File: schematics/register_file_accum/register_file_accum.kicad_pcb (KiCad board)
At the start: 2 copper layers, 100.1 x 91.1 mm, 31 parts, among them U1 74LS02, U2 74LS02, U3 74LS02, U4 74LS138, U5 74LS574, U6 74LS245, U7 74LS245, U8 74LS245

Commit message: silklayer check
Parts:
- moved kibuzzard-6911B41A 5.61 mm to (73.8, 78.8)

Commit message: power change
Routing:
- net GND: track 163.1 -> 190.3 mm
- net VCC: track 69.9 -> 94.1 mm, vias 1 -> 7

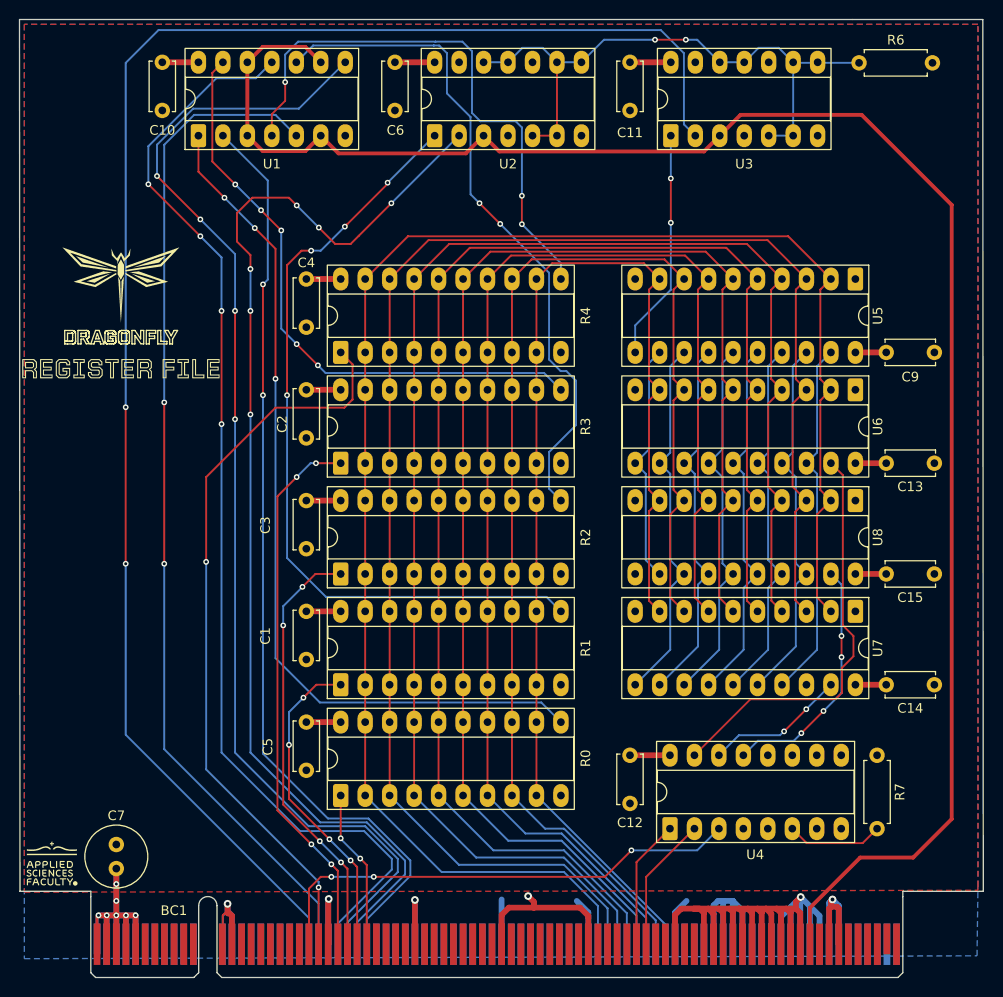
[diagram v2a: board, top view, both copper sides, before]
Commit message: fix: removed in control pins daisy chains
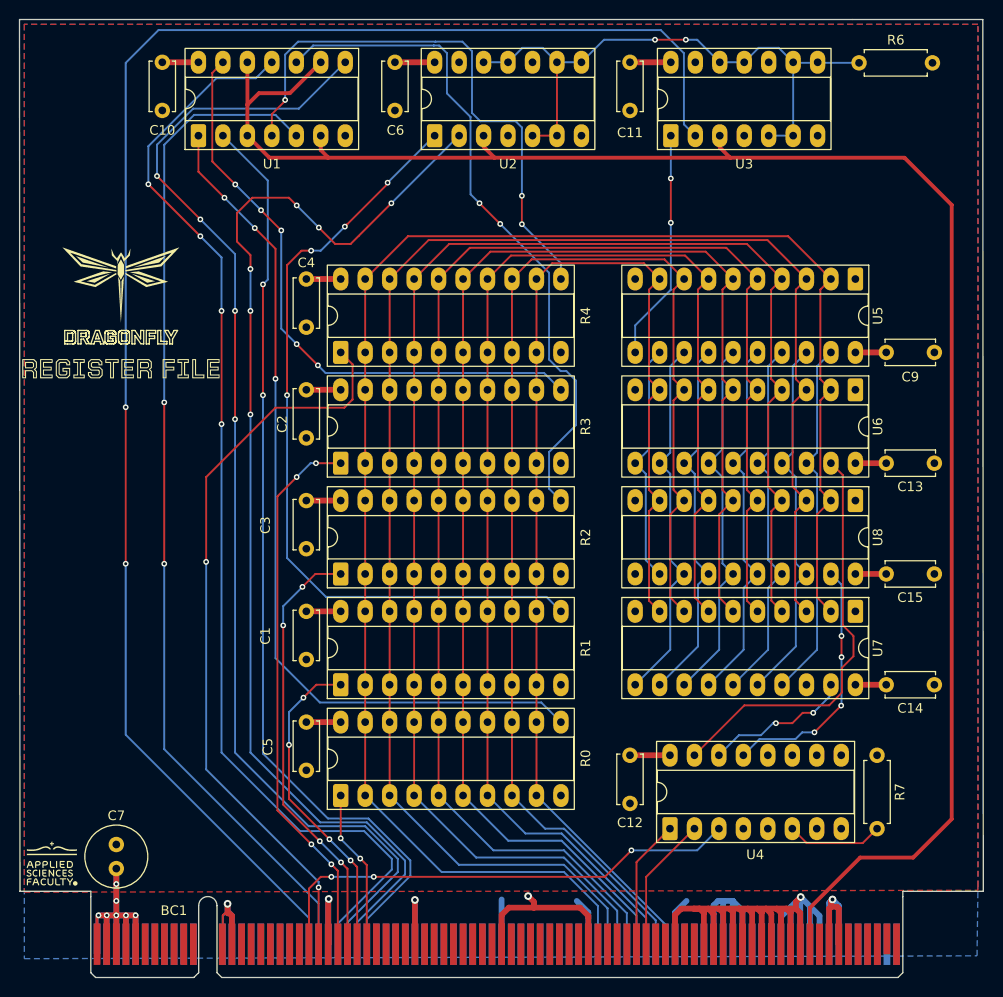
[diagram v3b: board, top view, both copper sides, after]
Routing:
- net /~{CLK}: track 184.7 -> 187.3 mm
- net /ACSHRIGHT: track 25.7 -> 26.4 mm
- net /ACSHLEFT: track 14.7 -> 15.3 mm

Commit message: fix(register_accum): fixed the data to y shape connection removed the vcc from the resistor
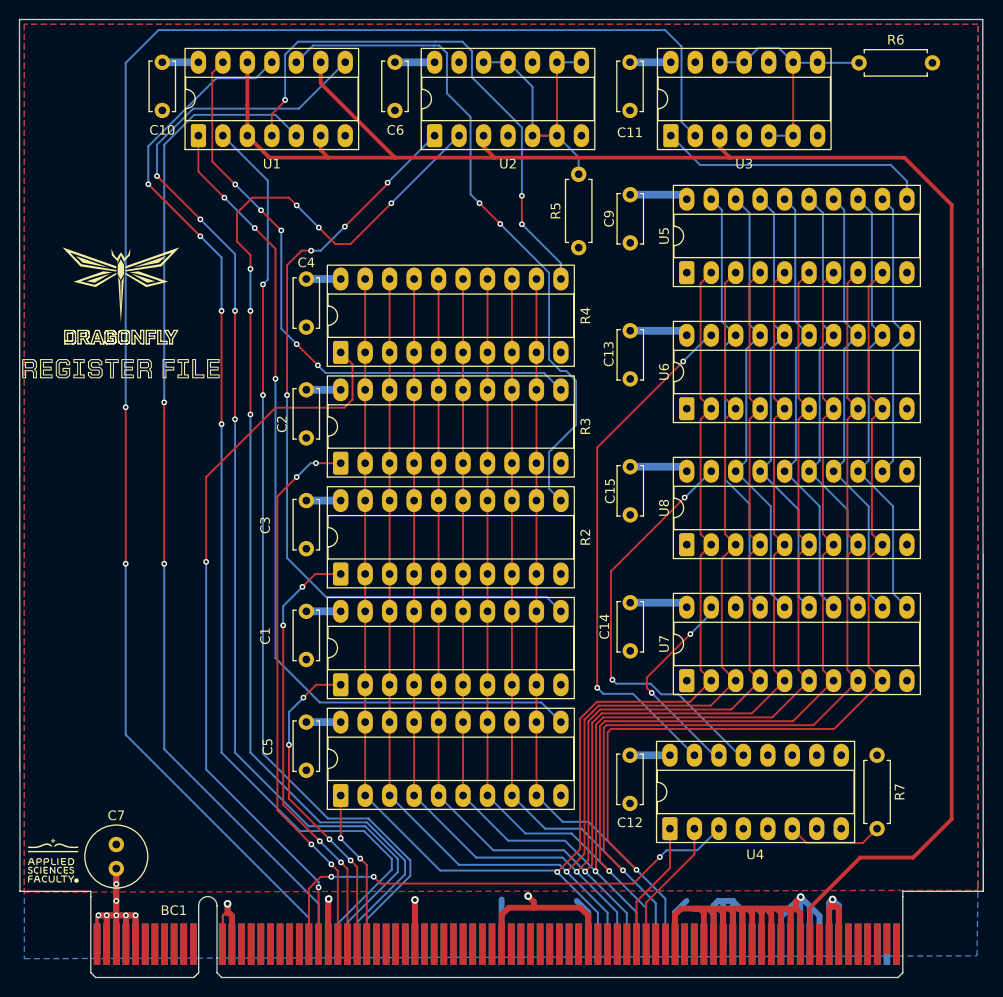
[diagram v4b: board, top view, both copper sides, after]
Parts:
- added R5: R, Resistor_THT:R_Axial_DIN0207_L6.3mm_D2.5mm_P7.62mm_Horizontal, F.Cu at (121.3, 66.2)
- moved C9 31.2 mm to (126.6, 60.7), turned to -90 degrees
- moved C13 29.9 mm to (126.6, 74.8), turned to -90 degrees
- moved C15 28.8 mm to (126.6, 88.9), turned to -90 degrees
- moved C14 27.9 mm to (126.6, 103.0), turned to -90 degrees
- moved U7 18.9 mm to (132.5, 111.1), turned to 90 degrees
- moved U8 18.1 mm to (132.5, 97.0), turned to 90 degrees
- moved U6 17.6 mm to (132.5, 82.9), turned to 90 degrees
- moved U5 17.5 mm to (132.5, 68.8), turned to 90 degrees
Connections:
- U2 pad 11: Net-(R6-Pad1) -> Net-(R5-Pad2)
- U2 pad 12: Net-(R6-Pad1) -> Net-(R5-Pad2)
- U2 pad 5: Net-(R6-Pad1) -> Net-(R5-Pad2)
- U2 pad 6: Net-(R6-Pad1) -> Net-(R5-Pad2)
- U2 pad 8: Net-(R6-Pad1) -> Net-(R5-Pad2)
- U2 pad 9: Net-(R6-Pad1) -> Net-(R5-Pad2)
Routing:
- net /DATA7: track 126.0 -> 168.1 mm, vias 0 -> 1
- net Net-(R6-Pad1): track 63.8 -> 25.9 mm, vias 2 -> 0
- net /DATA6: track 133.5 -> 166.6 mm, vias 0 -> 1
- net Net-(R5-Pad2): track 0.00 -> 31.0 mm
- net /DATA5: track 140.6 -> 165.4 mm, vias 0 -> 1
- net /ACSHRIGHT: track 26.4 -> 43.3 mm, vias 4 -> 2
- net /DATA4: track 147.7 -> 164.3 mm, vias 0 -> 1
- net /DATA0: track 176.1 -> 163.3 mm, vias 0 -> 1
- net /~{RAC}: track 43.3 -> 55.6 mm, vias 0 -> 2
- net VCC: track 94.1 -> 105.4 mm
- net /DATA3: track 154.5 -> 164.1 mm, vias 0 -> 1
- net /ACCUM1: track 38.7 -> 46.6 mm
- net /ACCUM5: track 38.7 -> 46.6 mm
- net /ACCUM4: track 38.7 -> 46.6 mm
- net /ACCUM3: track 38.7 -> 46.6 mm
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
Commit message: Add test points for register file + accum
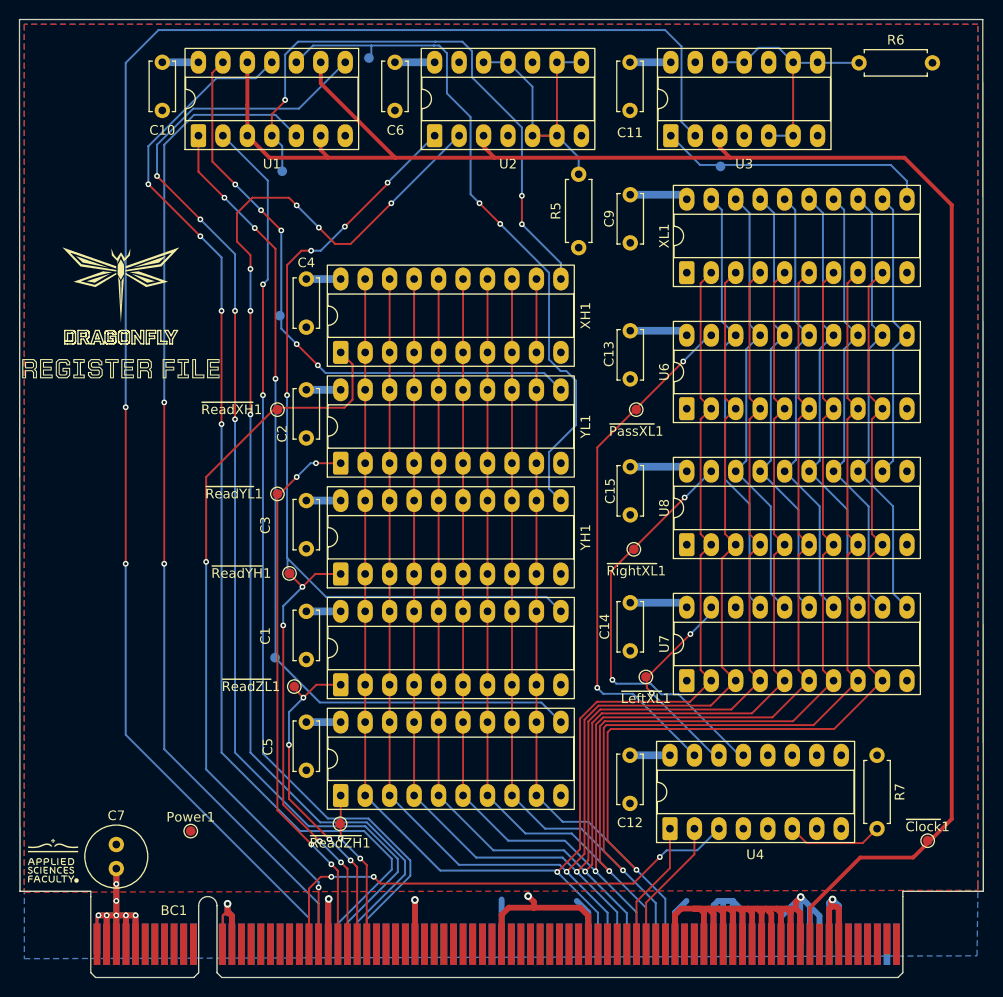
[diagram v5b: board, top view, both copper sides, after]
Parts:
- added Power1: Power, TestPoint:TestPoint_Pad_D1.0mm, F.Cu at (81.0, 126.8)
- added ~{Clock}1: ~{Clock}, TestPoint:TestPoint_Pad_D1.0mm, F.Cu at (157.5, 127.8)
- added ~{LeftXL}1: ~{LeftXL}, TestPoint:TestPoint_Pad_D1.0mm, F.Cu at (128.2, 110.8)
- added ~{LoadXH}1: ~{LoadXH}, TestPoint:TestPoint_Pad_D1.0mm, B.Cu at (90.5, 58.2)
- added ~{LoadXL}1: ~{LoadXL}, TestPoint:TestPoint_Pad_D1.0mm, B.Cu at (136.0, 57.8)
- added ~{LoadYH}1: ~{LoadYH}, TestPoint:TestPoint_Pad_D1.0mm, B.Cu at (99.5, 46.5)
- added ~{LoadYL}1: ~{LoadYL}, TestPoint:TestPoint_Pad_D1.0mm, B.Cu at (90.2, 73.2)
- added ~{LoadZH}1: ~{LoadZH}, TestPoint:TestPoint_Pad_D1.0mm, B.Cu at (89.8, 108.8)
- added ~{LoadZL}1: ~{LoadZL}, TestPoint:TestPoint_Pad_D1.0mm, B.Cu at (91.2, 100.0)
- added ~{PassXL}1: ~{PassXL}, TestPoint:TestPoint_Pad_D1.0mm, F.Cu at (127.2, 83.0)
- added ~{ReadXH}1: ~{ReadXH}, TestPoint:TestPoint_Pad_D1.0mm, F.Cu at (90.0, 83.0)
- added ~{ReadYH}1: ~{ReadYH}, TestPoint:TestPoint_Pad_D1.0mm, F.Cu at (91.2, 100.0)
- added ~{ReadYL}1: ~{ReadYL}, TestPoint:TestPoint_Pad_D1.0mm, F.Cu at (90.0, 91.8)
- added ~{ReadZH}1: ~{ReadZH}, TestPoint:TestPoint_Pad_D1.0mm, F.Cu at (96.5, 126.0)
- added ~{ReadZL}1: ~{ReadZL}, TestPoint:TestPoint_Pad_D1.0mm, F.Cu at (91.8, 111.8)
- added ~{RightXL}1: ~{RightXL}, TestPoint:TestPoint_Pad_D1.0mm, F.Cu at (127.0, 97.5)
- renumbered R4 to XH1, U5 to XL1, R2 to YH1, R3 to YL1, R0 to ZH1, R1 to ZL1
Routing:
- net Net-(XH1-Cp): track 56.8 -> 61.0 mm
- net Net-(BC1-~{RYH}): track 45.2 -> 47.2 mm
- net Net-(ZL1-Cp): track 82.4 -> 84.1 mm
- net Net-(BC1-~{RZL}): track 33.6 -> 34.9 mm
- net Net-(YH1-Cp): track 70.7 -> 72.0 mm

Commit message: Fix register file accum
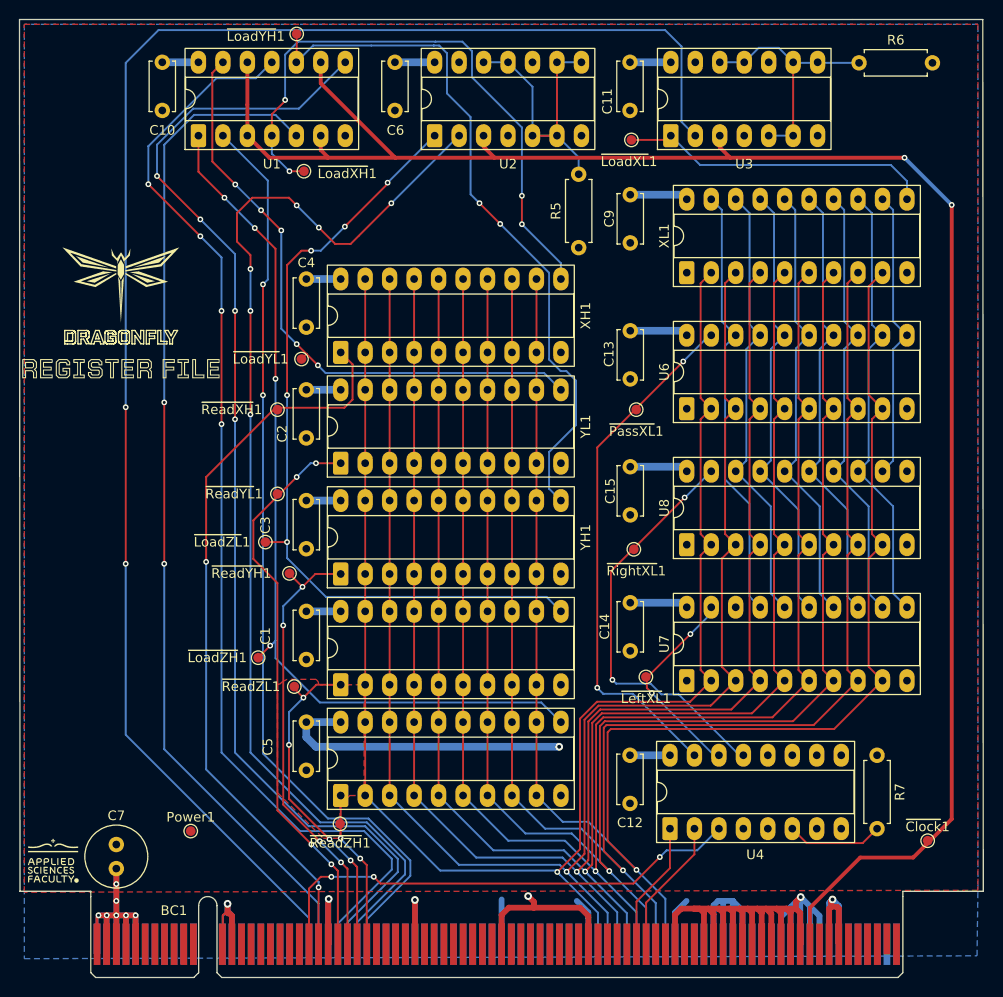
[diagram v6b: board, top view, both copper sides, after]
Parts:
- ~{LoadXH}1, ~{LoadXL}1, ~{LoadYH}1, ~{LoadYL}1, ~{LoadZH}1, ~{LoadZL}1: moved to F.Cu
- moved ~{LoadXL}1 9.65 mm to (126.8, 55.0), turned to 0 degrees
- moved ~{LoadYH}1 7.91 mm to (92.0, 44.0), turned to 0 degrees
- moved ~{LoadYL}1 5.03 mm to (92.5, 77.8), turned to 0 degrees
- moved ~{LoadZL}1 4.10 mm to (88.8, 96.8), turned to 0 degrees
- moved ~{LoadXH}1 2.25 mm to (92.8, 58.2), turned to 0 degrees
- moved ~{LoadZH}1 1.75 mm to (88.0, 108.8), turned to 0 degrees
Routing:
- net VCC: track 105.4 -> 133.6 mm, vias 7 -> 8
- net Net-(XL1-Cp): track 28.4 -> 32.6 mm
- net Net-(ZH1-Cp): track 89.9 -> 92.5 mm, vias 3 -> 4
- net Net-(BC1-~{RYL}): track 57.1 -> 59.2 mm
- net Net-(XH1-Cp): track 61.0 -> 62.8 mm, vias 3 -> 4
- net Net-(YH1-Cp): track 72.0 -> 73.7 mm
- net Net-(YL1-Cp): track 62.7 -> 63.5 mm
- net Net-(ZL1-Cp): track 84.1 -> 84.7 mm, vias 4 -> 5
- net /~{CLK}: vias 0 -> 2

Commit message: done
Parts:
- added kibuzzard-691DE19C: G***, kibuzzard-691DE19C, F.Cu at (67.0, 124.5)
- added kibuzzard-691DE1A7: G***, kibuzzard-691DE1A7, F.Cu at (156.0, 117.0)
- added kibuzzard-691DE1B7: G***, kibuzzard-691DE1B7, F.Cu at (66.5, 46.0)
